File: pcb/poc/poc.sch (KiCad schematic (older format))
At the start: 62 parts, among them J1 USB_B_Mini, J2 Right, J3 Left, J4 AVR-ISP-6, J5 Conn_02x10_Odd_Even, J6 Conn_02x08_Odd_Even, J7 Conn_01x02, J8 Conn_01x02, SW1 SW_Push, SW10 SW_Push_45deg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

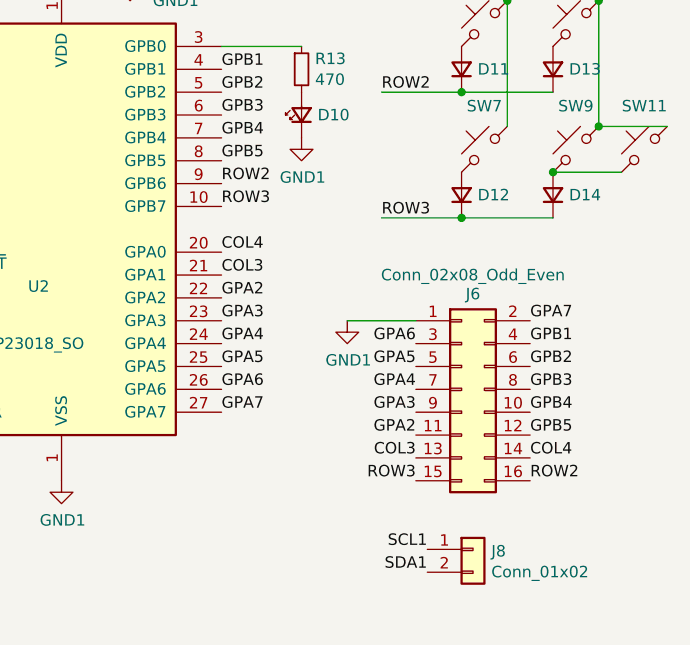
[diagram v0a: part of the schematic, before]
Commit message: pcb: poc: Space out left side
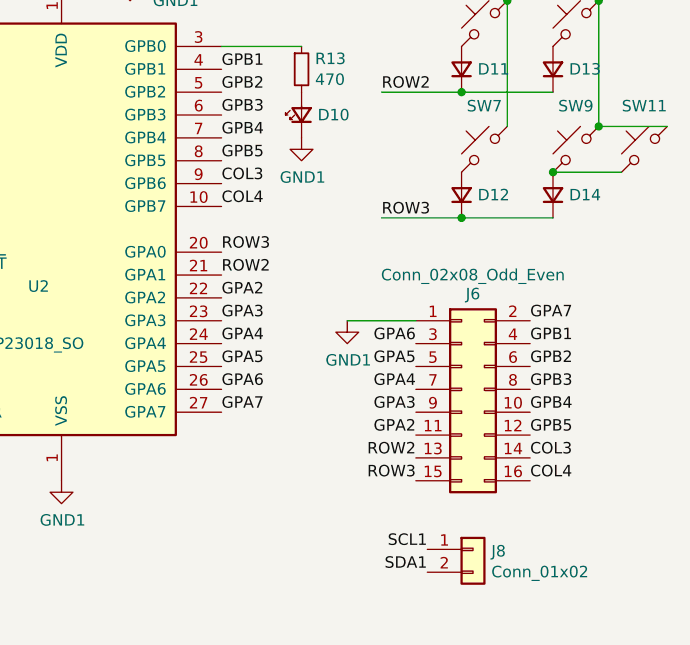
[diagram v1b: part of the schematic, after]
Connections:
- net COL3: now also J6.14 (Pin_14), U2.9 (GPB6); no longer J6.13 (Pin_13), U2.21 (GPA1)
- net COL4: now also J6.16 (Pin_16), U2.10 (GPB7); no longer J6.14 (Pin_14), U2.20 (GPA0)
- net ROW2: now also J6.13 (Pin_13), U2.21 (GPA1); no longer J6.16 (Pin_16), U2.9 (GPB6)
- net ROW3: now also U2.20 (GPA0); no longer U2.10 (GPB7)
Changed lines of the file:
@@
 Wire Wire Line
 	9700 4250 10100 4250
+Text Label 8650 4500 0    50   ~ 0
+ROW2
+Text Label 8650 4400 0    50   ~ 0
+ROW3
 Text Label 8650 4100 0    50   ~ 0
-ROW2
+COL3
 Text Label 8650 4200 0    50   ~ 0
-ROW3
-Text Label 8650 4500 0    50   ~ 0
-COL3
-Text Label 8650 4400 0    50   ~ 0
 COL4
 $Comp
@@
 Text Label 9550 5800 2    50   ~ 0
 SDA1
-Text Label 10000 5400 0    50   ~ 0
+Text Label 9500 5300 2    50   ~ 0
 ROW2
 Text Label 9500 5400 2    50   ~ 0
 ROW3
+Text Label 10000 5400 0    50   ~ 0
+COL4
 Text Label 10000 5300 0    50   ~ 0
-COL4
-Text Label 9500 5300 2    50   ~ 0
 COL3
 Text Label 10000 4800 0    50   ~ 0

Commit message: pcb: poc: Route left breakout
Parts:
- added J9: Conn_02x02_Odd_Even, Connector_PinSocket_2.54mm:PinSocket_2x02_P2.54mm_Vertical, symbol Connector_Generic:Conn_02x02_Odd_Even
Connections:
- net COL0: now also J9.2 (Pin_2); no longer J5.19 (Pin_19)
- net COL1: now also J9.1 (Pin_1); no longer J5.18 (Pin_18)
- net ROW0: now also J9.4 (Pin_4); no longer J5.17 (Pin_17)
- net ROW1: now also J9.3 (Pin_3); no longer J5.16 (Pin_16)
- no-connect marks 10 -> 14
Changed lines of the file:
@@
 Text Label 5300 5700 2    50   ~ 0
 PD6
-Text Label 5800 5700 0    50   ~ 0
+Text Label 5250 6800 2    50   ~ 0
 ROW1
-Text Label 5300 5800 2    50   ~ 0
+Text Label 5750 6800 0    50   ~ 0
 ROW0
-Text Label 5800 5800 0    50   ~ 0
+Text Label 5250 6700 2    50   ~ 0
 COL1
-Text Label 5300 5900 2    50   ~ 0
+Text Label 5750 6700 0    50   ~ 0
 COL0
 NoConn ~ 5800 5900
@@
 Text Label 9500 5200 2    50   ~ 0
 GPA2
+$Comp
+L Connector_Generic:Conn_02x02_Odd_Even J9
+U 1 1 60D2E9DB
+P 5450 6700
+F 0 "J9" H 5500 6917 50  0000 C CNN
+F 1 "Conn_02x02_Odd_Even" H 5500 6826 50  0000 C CNN
+F 2 "Connector_PinSocket_2.54mm:PinSocket_2x02_P2.54mm_Vertical" H 5450 6700 50  0001 C CNN
+F 3 "~" H 5450 6700 50  0001 C CNN
+	1    5450 6700
+	1    0    0    -1
+$EndComp
+NoConn ~ 5300 5900
+NoConn ~ 5300 5800
+NoConn ~ 5800 5800
+NoConn ~ 5800 5700
 $EndSCHEMATC

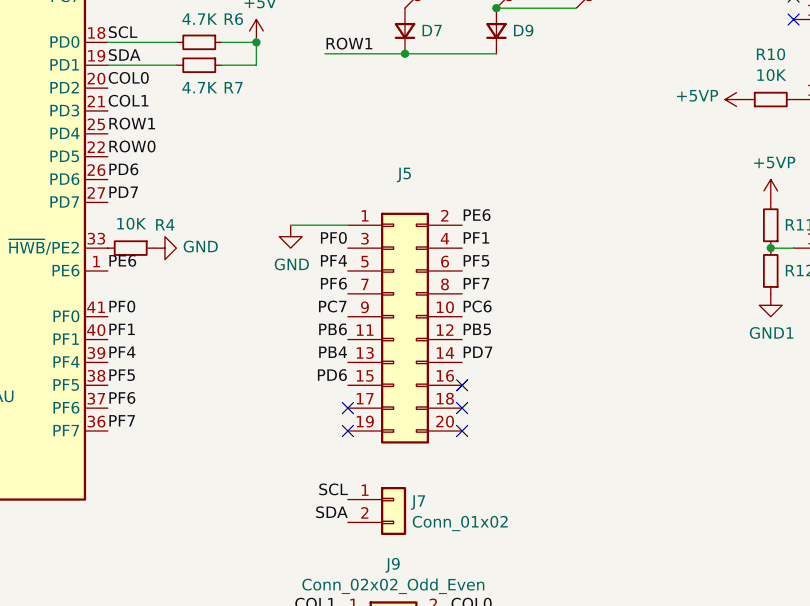
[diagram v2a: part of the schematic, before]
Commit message: pcb: poc: Make left breakout smaller
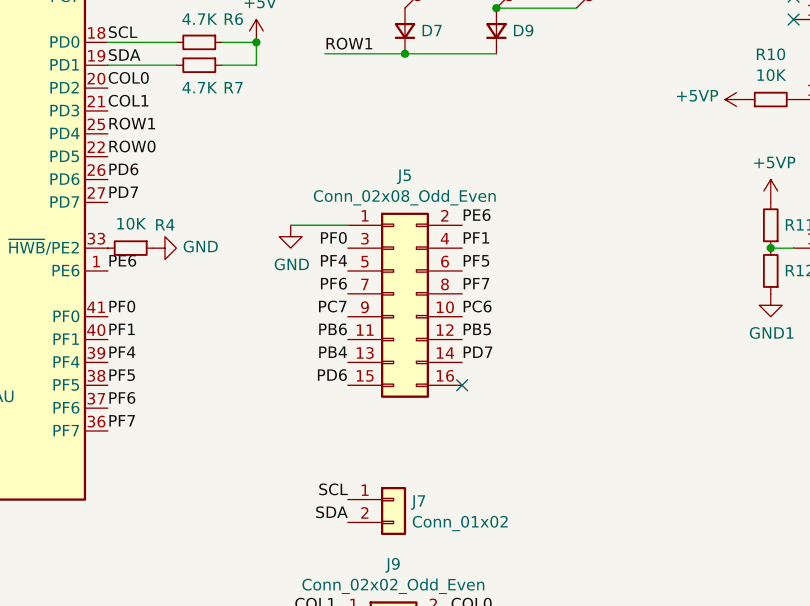
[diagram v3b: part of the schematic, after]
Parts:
- removed J5: Conn_02x10_Odd_Even, Connector_PinSocket_2.54mm:PinSocket_2x10_P2.54mm_Vertical, symbol Connector_Generic:Conn_02x10_Odd_Even
- added J5: Conn_02x08_Odd_Even, Connector_PinSocket_2.54mm:PinSocket_2x08_P2.54mm_Vertical, symbol Connector_Generic:Conn_02x08_Odd_Even
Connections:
- net GND: now also J5.1 (Pin_1)
- net PB4: now also J5.13 (Pin_13)
- net PB5: now also J5.12 (Pin_12)
- net PB6: now also J5.11 (Pin_11)
- net PC6: now also J5.10 (Pin_10)
- net PC7: now also J5.9 (Pin_9)
- net PD6: now also J5.15 (Pin_15)
- net PD7: now also J5.14 (Pin_14)
- net PE6: now also J5.2 (Pin_2)
- net PF0: now also J5.3 (Pin_3)
- net PF1: now also J5.4 (Pin_4)
- net PF4: now also J5.5 (Pin_5)
- net PF5: now also J5.6 (Pin_6)
- net PF6: now also J5.7 (Pin_7)
- net PF7: now also J5.8 (Pin_8)
- no-connect marks 14 -> 10
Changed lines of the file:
@@
-	1    0    0    -1
-$EndComp
-$Comp
-L Connector_Generic:Conn_02x10_Odd_Even J5
-U 1 1 604C9372
-P 5500 5400
-F 0 "J5" H 5550 6025 50  0000 C CNN
-F 1 "Conn_02x10_Odd_Even" H 5550 6026 50  0001 C CNN
-F 2 "Connector_PinSocket_2.54mm:PinSocket_2x10_P2.54mm_Vertical" H 5500 5400 50  0001 C CNN
-F 3 "~" H 5500 5400 50  0001 C CNN
-	1    5500 5400
 	1    0    0    -1
 $EndComp
@@
 Text Label 5750 6700 0    50   ~ 0
 COL0
-NoConn ~ 5800 5900
 $Comp
 L Connector_Generic:Conn_01x02 J7
@@
 	1    0    0    -1
 $EndComp
-NoConn ~ 5300 5900
-NoConn ~ 5300 5800
-NoConn ~ 5800 5800
 NoConn ~ 5800 5700
+$Comp
+L Connector_Generic:Conn_02x08_Odd_Even J5
+U 1 1 60D61D34
+P 5500 5300
+F 0 "J5" H 5550 5817 50  0000 C CNN
+F 1 "Conn_02x08_Odd_Even" H 5550 5726 50  0000 C CNN
+F 2 "Connector_PinSocket_2.54mm:PinSocket_2x08_P2.54mm_Vertical" H 5500 5300 50  0001 C CNN
+F 3 "~" H 5500 5300 50  0001 C CNN
+	1    5500 5300
+	1    0    0    -1
+$EndComp
 $EndSCHEMATC

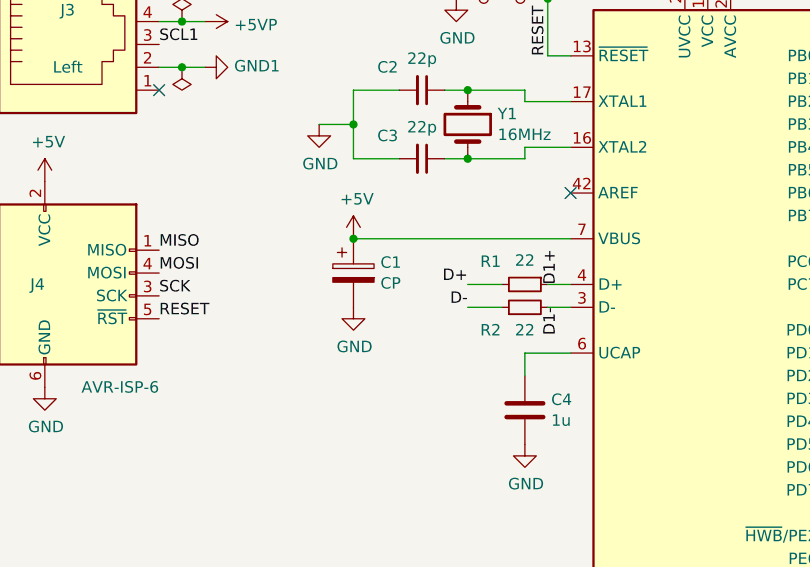
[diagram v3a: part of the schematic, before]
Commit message: pcb: poc: annotate capacitor
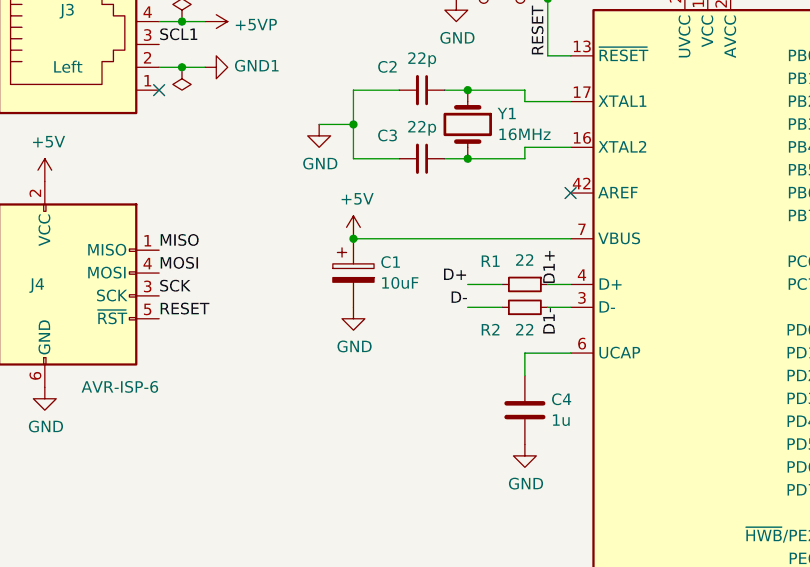
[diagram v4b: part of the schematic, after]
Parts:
- C1: value CP -> 10uF
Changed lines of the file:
@@
 P 2100 3950
 F 0 "C1" H 2218 3996 50  0000 L CNN
-F 1 "CP" H 2218 3905 50  0000 L CNN
+F 1 "10uF" H 2218 3905 50  0000 L CNN
 F 2 "Capacitor_Tantalum_SMD:CP_EIA-3216-18_Kemet-A_Pad1.58x1.35mm_HandSolder" H 2138 3800 50  0001 C CNN
 F 3 "~" H 2100 3950 50  0001 C CNN
